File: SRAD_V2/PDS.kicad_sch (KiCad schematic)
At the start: 10 parts, among them U12 TPS563200

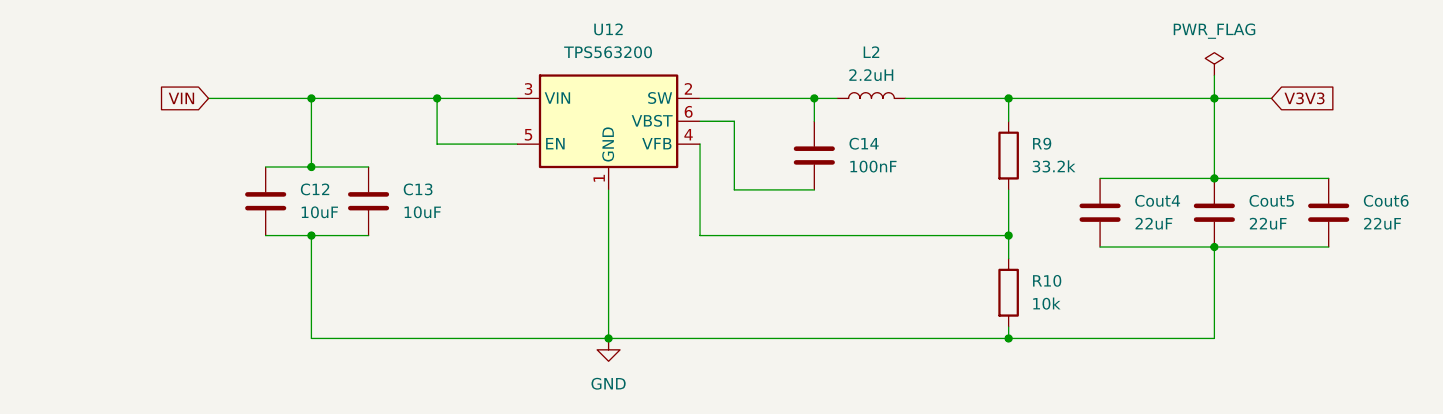
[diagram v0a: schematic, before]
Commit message: created some basic building blocks as hierarchical sheets
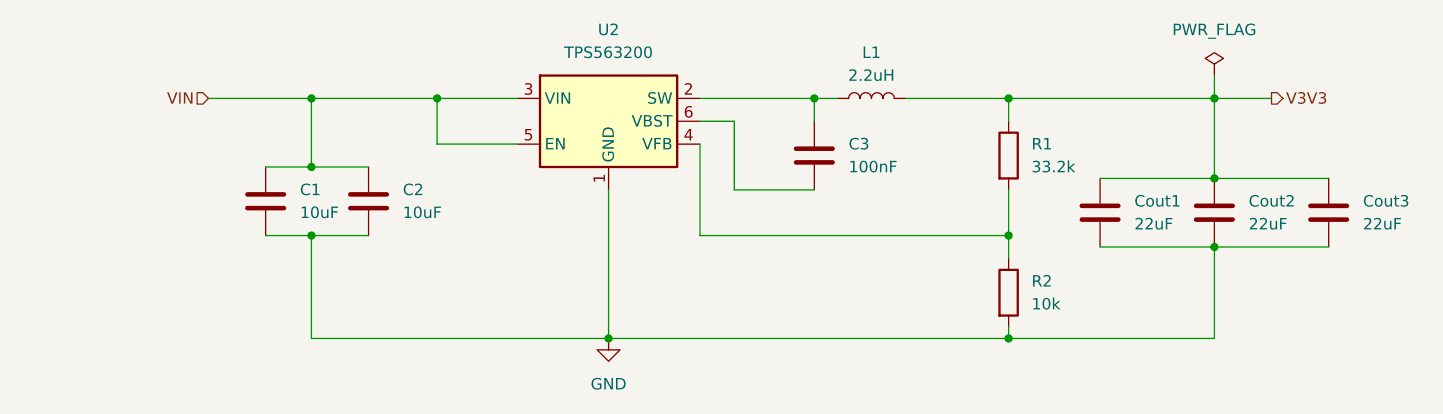
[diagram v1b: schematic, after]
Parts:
- renumbered C12 to C1, C13 to C2, C14 to C3, Cout4 to Cout1, Cout5 to Cout2, Cout6 to Cout3, L2 to L1, R9 to R1, R10 to R2, U12 to U2
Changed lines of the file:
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@@
 		)
 	)
-	(global_label "VIN"
+	(hierarchical_label "VIN"
 		(shape input)
 		(at 92.71 81.28 180)
-		(fields_autoplaced yes)
 		(effects
 			(font
@@
 			(justify right)
 		)
-		(property "Intersheetrefs" "${INTERSHEET_REFS}"
-			(at 86.7009 81.28 0)
-			(show_name yes)
-			(effects
-				(font
-					(size 1.27 1.27)
-				)
-				(justify right)
-				(hide yes)
-			)
-		)
-	)
-	(global_label "V3V3"
-		(shape input)
+	)
+	(hierarchical_label "V3V3"
+		(shape output)
 		(at 210.82 81.28 0)
-		(fields_autoplaced yes)
 		(effects
 			(font
@@
 			(justify left)
 		)
-		(property "Intersheetrefs" "${INTERSHEET_REFS}"
-			(at 218.4014 81.28 0)
-			(show_name yes)
-			(effects
-				(font
-					(size 1.27 1.27)
-				)
-				(justify left)
-				(hide yes)
-			)
-		)
 	)
 	(symbol
@@
 		(dnp no)
 		(fields_autoplaced yes)
-		(property "Reference" "#FLG02"
+		(property "Reference" "#FLG01"
 			(at 204.47 76.835 0)
 			(effects
@@
 			(project "SRAD_V2"
 				(path "/016ea6e5-09c6-43d4-b6cc-3404e2d65458/9c8bbba4-8714-49e8-941c-914b77648ac5"
-					(reference "#FLG02")
+					(reference "#FLG01")
 					(unit 1)
 				)
@@
 		(dnp no)
 		(fields_autoplaced yes)
-		(property "Reference" "Cout6"
+		(property "Reference" "Cout3"
 			(at 220.98 92.7099 0)
 			(effects
@@
 			(project "SRAD_V2"
 				(path "/016ea6e5-09c6-43d4-b6cc-3404e2d65458/9c8bbba4-8714-49e8-941c-914b77648ac5"
-					(reference "Cout6")
+					(reference "Cout3")
 					(unit 1)
 				)
@@
 		(dnp no)
 		(fields_autoplaced yes)
-		(property "Reference" "L2"
+		(property "Reference" "L1"
 			(at 166.37 76.2 90)
 			(effects
@@
 			(project "SRAD_V2"
 				(path "/016ea6e5-09c6-43d4-b6cc-3404e2d65458/9c8bbba4-8714-49e8-941c-914b77648ac5"
-					(reference "L2")
+					(reference "L1")
 					(unit 1)
 				)
@@
 		(dnp no)
 		(fields_autoplaced yes)
-		(property "Reference" "#PWR022"
+		(property "Reference" "#PWR01"
 			(at 137.16 114.3 0)
 			(effects
@@
 			(project "SRAD_V2"
 				(path "/016ea6e5-09c6-43d4-b6cc-3404e2d65458/9c8bbba4-8714-49e8-941c-914b77648ac5"
-					(reference "#PWR022")
+					(reference "#PWR01")
 					(unit 1)
 				)
@@
 		(dnp no)
 		(fields_autoplaced yes)
-		(property "Reference" "U12"
+		(property "Reference" "U2"
 			(at 137.16 73.66 0)
 			(effects
@@
 			(project "SRAD_V2"
 				(path "/016ea6e5-09c6-43d4-b6cc-3404e2d65458/9c8bbba4-8714-49e8-941c-914b77648ac5"
-					(reference "U12")
+					(reference "U2")
 					(unit 1)
 				)
@@
 		(on_board yes)
 		(dnp no)
-		(property "Reference" "Cout4"
+		(property "Reference" "Cout1"
 			(at 195.58 92.7099 0)
 			(effects
@@
 			(project "SRAD_V2"
 				(path "/016ea6e5-09c6-43d4-b6cc-3404e2d65458/9c8bbba4-8714-49e8-941c-914b77648ac5"
-					(reference "Cout4")
+					(reference "Cout1")
 					(unit 1)
 				)
@@
 		(dnp no)
 		(fields_autoplaced yes)
-		(property "Reference" "C14"
+		(property "Reference" "C3"
 			(at 163.83 86.3599 0)
 			(effects
@@
 			(project "SRAD_V2"
 				(path "/016ea6e5-09c6-43d4-b6cc-3404e2d65458/9c8bbba4-8714-49e8-941c-914b77648ac5"
-					(reference "C14")
+					(reference "C3")
 					(unit 1)
 				)
@@
 		(dnp no)
 		(fields_autoplaced yes)
-		(property "Reference" "R10"
+		(property "Reference" "R2"
 			(at 184.15 101.5999 0)
 			(effects
@@
 			(project "SRAD_V2"
 				(path "/016ea6e5-09c6-43d4-b6cc-3404e2d65458/9c8bbba4-8714-49e8-941c-914b77648ac5"
-					(reference "R10")
+					(reference "R2")
 					(unit 1)
 				)
@@
 		(dnp no)
 		(fields_autoplaced yes)
-		(property "Reference" "R9"
+		(property "Reference" "R1"
 			(at 184.15 86.3599 0)
 			(effects
@@
 			(project "SRAD_V2"
 				(path "/016ea6e5-09c6-43d4-b6cc-3404e2d65458/9c8bbba4-8714-49e8-941c-914b77648ac5"
-					(reference "R9")
+					(reference "R1")
 					(unit 1)
 				)
@@
 		(dnp no)
 		(fields_autoplaced yes)
-		(property "Reference" "C12"
+		(property "Reference" "C1"
 			(at 102.87 91.4399 0)
 			(effects
@@
 			(project "SRAD_V2"
 				(path "/016ea6e5-09c6-43d4-b6cc-3404e2d65458/9c8bbba4-8714-49e8-941c-914b77648ac5"
-					(reference "C12")
+					(reference "C1")
 					(unit 1)
 				)
@@
 		(dnp no)
 		(fields_autoplaced yes)
-		(property "Reference" "Cout5"
+		(property "Reference" "Cout2"
 			(at 208.28 92.7099 0)
 			(effects
@@
 			(project "SRAD_V2"
 				(path "/016ea6e5-09c6-43d4-b6cc-3404e2d65458/9c8bbba4-8714-49e8-941c-914b77648ac5"
-					(reference "Cout5")
+					(reference "Cout2")
 					(unit 1)
 				)
@@
 		(dnp no)
 		(fields_autoplaced yes)
-		(property "Reference" "C13"
+		(property "Reference" "C2"
 			(at 114.3 91.4399 0)
 			(effects
@@
 			(project "SRAD_V2"
 				(path "/016ea6e5-09c6-43d4-b6cc-3404e2d65458/9c8bbba4-8714-49e8-941c-914b77648ac5"
-					(reference "C13")
-					(unit 1)
-				)
+					(reference "C2")
+					(unit 1)
+				)

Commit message: linked 3-d models
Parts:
- L1: footprint VLS6045EX-2R2N:IND_VLS6045EX-2R2N -> Inductor:IND_VLS6045EX-2R2N
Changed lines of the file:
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@@
 			)
 		)
-		(property "Footprint" "VLS6045EX-2R2N:IND_VLS6045EX-2R2N"
+		(property "Footprint" "Inductor:IND_VLS6045EX-2R2N"
 			(at 166.37 81.28 0)
 			(effects

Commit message: more changes
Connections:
- net V3V3 renamed +3V3
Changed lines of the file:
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@@
-	(wire
-		(pts
-			(xy 204.47 78.74) (xy 204.47 81.28)
-		)
-		(stroke
-			(width 0)
-			(type default)
-		)
-	)
 	(wire
 		(pts
@@
 		)
 	)
-	(hierarchical_label "V3V3"
+	(hierarchical_label "+3V3"
 		(shape output)
 		(at 210.82 81.28 0)
@@
 		)
 	)
-	(symbol
-		(lib_id "power:PWR_FLAG")
-		(at 204.47 78.74 0)
-		(unit 1)
-		(exclude_from_sim no)
-		(in_bom yes)
-		(on_board yes)
-		(dnp no)
-		(fields_autoplaced yes)
-		(property "Reference" "#FLG01"
-			(at 204.47 76.835 0)
-			(effects
-				(font
-					(size 1.27 1.27)
-				)
-				(hide yes)
-			)
-		)
-		(property "Value" "PWR_FLAG"
-			(at 204.47 73.66 0)
-			(effects
-				(font
-					(size 1.27 1.27)
-				)
-			)
-		)
-		(property "Footprint" ""
-			(at 204.47 78.74 0)
-			(effects
-				(font
-					(size 1.27 1.27)
-				)
-				(hide yes)
-			)
-		)
-		(property "Datasheet" "~"
-			(at 204.47 78.74 0)
-			(effects
-				(font
-					(size 1.27 1.27)
-				)
-				(hide yes)
-			)
-		)
-		(property "Description" "Special symbol for telling ERC where power comes from"
-			(at 204.47 78.74 0)
-			(effects
-				(font
-					(size 1.27 1.27)
-				)
-				(hide yes)
-			)
-		)
-		(pin "1"
-		)
-		(instances
-			(project "SRAD_V2"
-				(path "/016ea6e5-09c6-43d4-b6cc-3404e2d65458/9c8bbba4-8714-49e8-941c-914b77648ac5"
-					(reference "#FLG01")
-					(unit 1)
-				)
-			)
-		)
-	)

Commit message: fixed some origin issues on pcb -- working on the PDS
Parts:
- added Cout4: 0.1uF, Capacitor_SMD:C_0603_1608Metric, symbol Device:C
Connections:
- net GND: now also Cout4.2
- net VIN: now also Cout4.1
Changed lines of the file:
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@@
+	)
+	(junction
+		(at 86.36 81.28)
+		(diameter 0)
+		(color 0 0 0 0)
 	)
 	(junction
@@
 	)
 	(junction
+		(at 104.14 107.95)
+		(diameter 0)
+		(color 0 0 0 0)
+	)
+	(junction
 		(at 104.14 88.9)
 		(diameter 0)
@@
 	(wire
 		(pts
+			(xy 86.36 107.95) (xy 104.14 107.95)
+		)
+		(stroke
+			(width 0)
+			(type default)
+		)
+	)
+	(wire
+		(pts
 			(xy 104.14 107.95) (xy 104.14 96.52)
 		)
@@
 	(wire
 		(pts
+			(xy 86.36 81.28) (xy 104.14 81.28)
+		)
+		(stroke
+			(width 0)
+			(type default)
+		)
+	)
+	(wire
+		(pts
+			(xy 86.36 96.52) (xy 86.36 107.95)
+		)
+		(stroke
+			(width 0)
+			(type default)
+		)
+	)
+	(wire
+		(pts
 			(xy 204.47 97.79) (xy 204.47 107.95)
 		)
@@
 	(wire
 		(pts
-			(xy 92.71 81.28) (xy 104.14 81.28)
+			(xy 77.47 81.28) (xy 86.36 81.28)
 		)
 		(stroke
@@
 		(pts
 			(xy 99.06 88.9) (xy 104.14 88.9)
+		)
+		(stroke
+			(width 0)
+			(type default)
+		)
+	)
+	(wire
+		(pts
+			(xy 86.36 81.28) (xy 86.36 88.9)
 		)
 		(stroke
@@
 	(hierarchical_label "VIN"
 		(shape input)
-		(at 92.71 81.28 180)
+		(at 77.47 81.28 180)
 		(effects
 			(font
@@
 					(unit 1)
 				)
+			)
+		)
+	)
+	(symbol
+		(lib_id "Device:C")
+		(at 86.36 92.71 0)
+		(unit 1)
+		(exclude_from_sim no)
+		(in_bom yes)
+		(on_board yes)
+		(dnp no)
+		(fields_autoplaced yes)
+		(property "Reference" "Cout4"
+			(at 90.17 91.4399 0)
+			(effects
+				(font
+					(size 1.27 1.27)
+				)
+				(justify left)
+			)
+		)
+		(property "Value" "0.1uF"
+			(at 90.17 93.9799 0)
+			(effects
+				(font
+					(size 1.27 1.27)
+				)
+				(justify left)
+			)
+		)
+		(property "Footprint" "Capacitor_SMD:C_0603_1608Metric"
+			(at 87.3252 96.52 0)
+			(effects
+				(font
+					(size 1.27 1.27)
+				)
+				(hide yes)
+			)
+		)
+		(property "Datasheet" "~"
+			(at 86.36 92.71 0)
+			(effects
+				(font
+					(size 1.27 1.27)
+				)
+				(hide yes)
+			)
+		)
+		(property "Description" "Unpolarized capacitor"
+			(at 86.36 92.71 0)
+			(effects
+				(font
+					(size 1.27 1.27)
+				)
+				(hide yes)
+			)
+		)
+		(pin "1"
+		)
+		(pin "2"
+		)
+		(instances
+			(project "SRAD_V2"
+				(path "/016ea6e5-09c6-43d4-b6cc-3404e2d65458/9c8bbba4-8714-49e8-941c-914b77648ac5"
+					(reference "Cout4")
+					(unit 1)
+				)

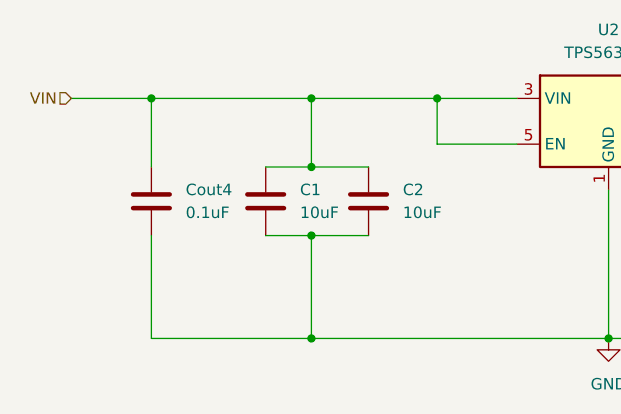
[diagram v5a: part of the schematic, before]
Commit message: sensor routing
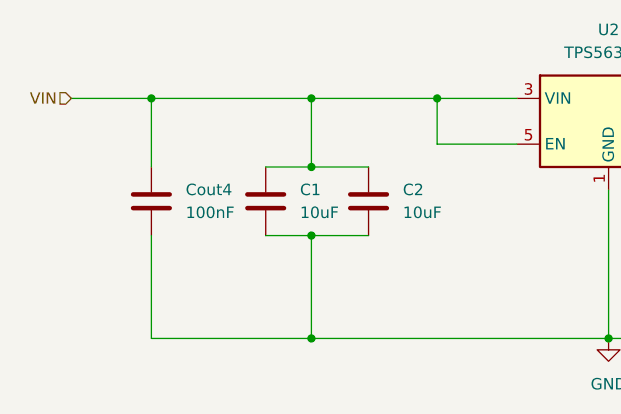
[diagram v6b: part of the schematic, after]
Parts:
- Cout4: value 0.1uF -> 100nF
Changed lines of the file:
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@@
 			)
 		)
-		(property "Value" "0.1uF"
+		(property "Value" "100nF"
 			(at 90.17 93.9799 0)
 			(show_name no)

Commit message: more routing
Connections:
- net +3V3 renamed +3.3V
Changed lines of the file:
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@@
+		)
+	)
+	(label "+BATT"
+		(at 97.79 81.28 0)
+		(effects
+			(font
+				(size 1.27 1.27)
+			)
+			(justify left bottom)
 		)
 	)
@@
 		)
 	)
-	(hierarchical_label "+3V3"
+	(hierarchical_label "+3.3V"
 		(shape output)
 		(at 210.82 81.28 0)
